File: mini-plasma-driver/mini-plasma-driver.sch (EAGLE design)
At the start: 82 parts, among them IC1 IR21844D, IC2 74LS19N, IC3 NE555N, IC4 NCP781IC, IC5 IR21844D, Q1 IRF640, Q2 IRF640, Q3 2N2369, Q4 2N2369, Q5 IRF640, Q6 IRF640

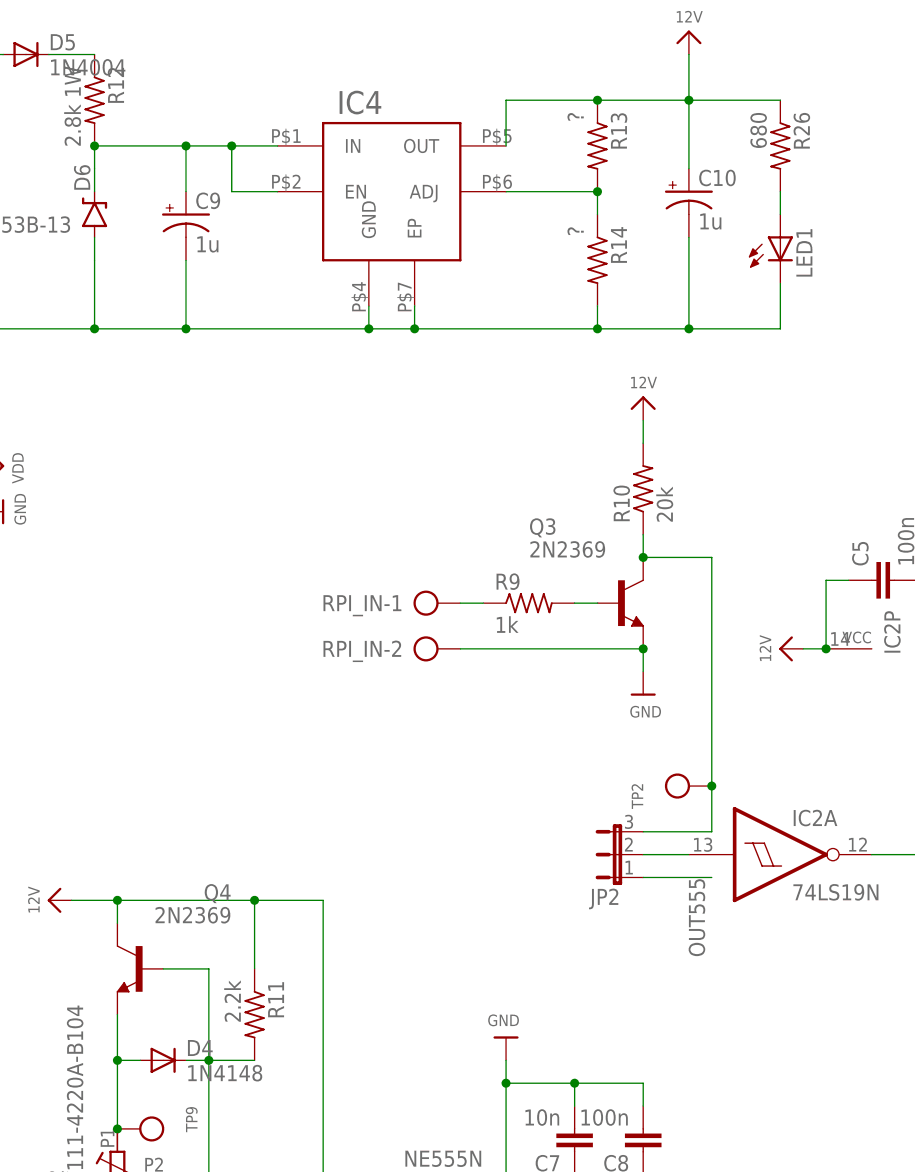
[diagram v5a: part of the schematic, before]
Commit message: C9 and C10 are not polarized
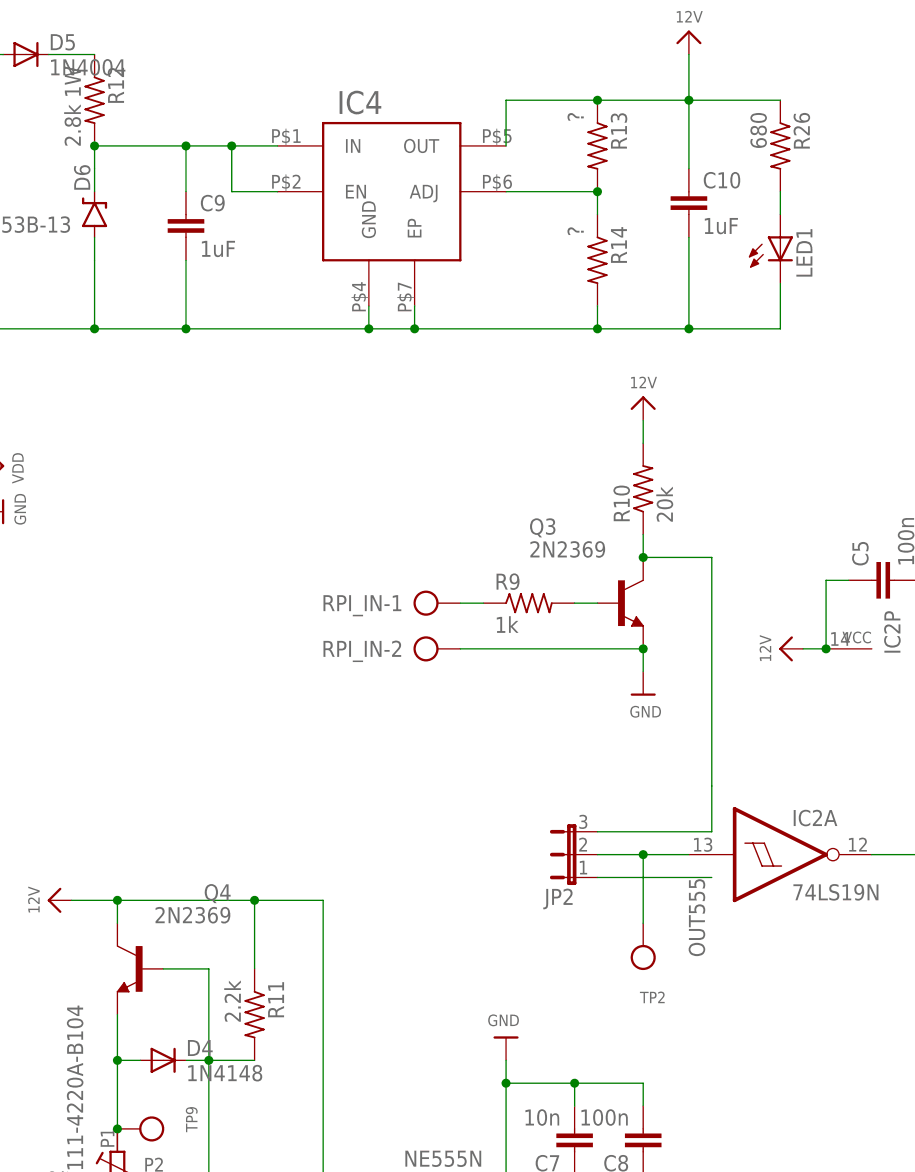
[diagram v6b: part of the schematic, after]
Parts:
- C10, C9: value 1u -> 1uF; device rcl:CPOL-USE2.5-5 -> rcl:C-EU025-025X050
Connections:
- net 12V: now also C10.1; no longer C10.+
- net GND: now also C10.2, C9.2; no longer C10.-, C9.-
- net N$12: no longer TP2.P$1
- net N$13: now also TP2.P$1
- net N$20: now also C9.1; no longer C9.+
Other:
- moved on the sheet: JP2, TP2
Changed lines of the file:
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@@
 <part name="GND3" library="microbuilder" deviceset="GND" device=""/>
 <part name="JP2" library="jumper" library_urn="urn:adsk.eagle:library:252" deviceset="JP2E" device="" package3d_urn="urn:adsk.eagle:package:15452/1"/>
-<part name="TP2" library="microbuilder" deviceset="TESTPOINT" device="0.1&quot;"/>
 <part name="IC2" library="74xx-eu" library_urn="urn:adsk.eagle:library:85" deviceset="74*19" device="N" package3d_urn="urn:adsk.eagle:package:2008/1" technology="LS"/>
 <part name="C5" library="rcl" library_urn="urn:adsk.eagle:library:334" deviceset="C-EU" device="025-025X050" package3d_urn="urn:adsk.eagle:package:23629/2" value="100n"/>
@@
 <part name="R12" library="rcl" library_urn="urn:adsk.eagle:library:334" deviceset="R-US_" device="0207/10" package3d_urn="urn:adsk.eagle:package:23491/1" value="2.8k 1W"/>
 <part name="D6" library="SparkFun-DiscreteSemi" deviceset="DIODE-ZENER" device="SMB" value="1SMB5953B-13"/>
-<part name="C9" library="rcl" library_urn="urn:adsk.eagle:library:334" deviceset="CPOL-US" device="E2.5-5" package3d_urn="urn:adsk.eagle:package:23344/1" value="1u"/>
 <part name="R13" library="rcl" library_urn="urn:adsk.eagle:library:334" deviceset="R-US_" device="0207/10" package3d_urn="urn:adsk.eagle:package:23491/1" value="?"/>
 <part name="R14" library="rcl" library_urn="urn:adsk.eagle:library:334" deviceset="R-US_" device="0207/10" package3d_urn="urn:adsk.eagle:package:23491/1" value="?"/>
-<part name="C10" library="rcl" library_urn="urn:adsk.eagle:library:334" deviceset="CPOL-US" device="E2.5-5" package3d_urn="urn:adsk.eagle:package:23344/1" value="1u"/>
 <part name="12V7" library="microbuilder" deviceset="12V" device=""/>
 <part name="GND7" library="microbuilder" deviceset="GND" device=""/>
@@
 <part name="TP8" library="microbuilder" deviceset="TESTPOINT" device="0.1&quot;"/>
 <part name="TP9" library="microbuilder" deviceset="TESTPOINT" device="0.1&quot;"/>
+<part name="TP2" library="microbuilder" deviceset="TESTPOINT" device="0.1&quot;"/>
+<part name="C9" library="rcl" library_urn="urn:adsk.eagle:library:334" deviceset="C-EU" device="025-025X050" package3d_urn="urn:adsk.eagle:package:23629/2" value="1uF"/>
+<part name="C10" library="rcl" library_urn="urn:adsk.eagle:library:334" deviceset="C-EU" device="025-025X050" package3d_urn="urn:adsk.eagle:package:23629/2" value="1uF"/>
 </parts>
 <sheets>
@@
 <instance part="12V3" gate="G$1" x="0" y="99.06"/>
 <instance part="GND3" gate="G$1" x="0" y="66.04"/>
-<instance part="JP2" gate="1" x="-2.54" y="48.26" rot="R90"/>
-<instance part="TP2" gate="G$1" x="7.62" y="55.88" rot="R90"/>
+<instance part="JP2" gate="1" x="-7.62" y="48.26" rot="R90"/>
 <instance part="IC2" gate="A" x="15.24" y="48.26"/>
 <instance part="IC2" gate="B" x="43.18" y="-10.16"/>
@@
 <attribute name="VALUE" x="-63.5" y="119.1514" size="1.778" layer="96" rot="R180"/>
 </instance>
-<instance part="C9" gate="G$1" x="-50.8" y="119.38"/>
 <instance part="R13" gate="G$1" x="-5.08" y="127" rot="R270"/>
 <instance part="R14" gate="G$1" x="-5.08" y="114.3" rot="R270"/>
-<instance part="C10" gate="G$1" x="5.08" y="121.92"/>
 <instance part="12V7" gate="G$1" x="5.08" y="139.7"/>
 <instance part="GND7" gate="G$1" x="-83.82" y="104.14"/>
@@
 <instance part="TP8" gate="G$1" x="-58.42" y="2.54" rot="R270"/>
 <instance part="TP9" gate="G$1" x="-58.42" y="17.78" rot="R270"/>
+<instance part="TP2" gate="G$1" x="0" y="40.64" rot="R180"/>
+<instance part="C9" gate="G$1" x="-50.8" y="119.38"/>
+<instance part="C10" gate="G$1" x="5.08" y="121.92"/>
 </instances>
 <busses>
@@
 <wire x1="-5.08" y1="132.08" x2="-15.24" y2="132.08" width="0.1524" layer="91"/>
 <wire x1="-15.24" y1="132.08" x2="-15.24" y2="127" width="0.1524" layer="91"/>
-<pinref part="C10" gate="G$1" pin="+"/>
 <wire x1="5.08" y1="124.46" x2="5.08" y2="132.08" width="0.1524" layer="91"/>
 <pinref part="R13" gate="G$1" pin="1"/>
@@
 <pinref part="R26" gate="G$1" pin="1"/>
 <wire x1="5.08" y1="132.08" x2="15.24" y2="132.08" width="0.1524" layer="91"/>
+<pinref part="C10" gate="G$1" pin="1"/>
 </segment>
 <segment>
@@
 <wire x1="-30.48" y1="109.22" x2="-30.48" y2="106.68" width="0.1524" layer="91"/>
 <wire x1="-60.96" y1="114.3" x2="-60.96" y2="106.68" width="0.1524" layer="91"/>
-<pinref part="C9" gate="G$1" pin="-"/>
 <wire x1="-50.8" y1="114.3" x2="-50.8" y2="106.68" width="0.1524" layer="91"/>
-<pinref part="C10" gate="G$1" pin="-"/>
 <wire x1="5.08" y1="116.84" x2="5.08" y2="106.68" width="0.1524" layer="91"/>
 <wire x1="5.08" y1="106.68" x2="-5.08" y2="106.68" width="0.1524" layer="91"/>
@@
 <wire x1="15.24" y1="106.68" x2="15.24" y2="111.76" width="0.1524" layer="91"/>
 <junction x="5.08" y="106.68"/>
+<pinref part="C9" gate="G$1" pin="2"/>
+<pinref part="C10" gate="G$1" pin="2"/>
 </segment>
 <segment>
@@
 <pinref part="JP2" gate="1" pin="3"/>
 <wire x1="7.62" y1="55.88" x2="7.62" y2="50.8" width="0.1524" layer="91"/>
-<wire x1="7.62" y1="50.8" x2="0" y2="50.8" width="0.1524" layer="91"/>
-<pinref part="TP2" gate="G$1" pin="P$1"/>
-<junction x="7.62" y="55.88"/>
+<wire x1="7.62" y1="50.8" x2="-5.08" y2="50.8" width="0.1524" layer="91"/>
 <junction x="0" y="81.28"/>
 </segment>
@@
 <wire x1="5.08" y1="48.26" x2="0" y2="48.26" width="0.1524" layer="91"/>
 <pinref part="IC2" gate="A" pin="I"/>
+<wire x1="0" y1="48.26" x2="-5.08" y2="48.26" width="0.1524" layer="91"/>
+<pinref part="TP2" gate="G$1" pin="P$1"/>
+<wire x1="0" y1="40.64" x2="0" y2="48.26" width="0.1524" layer="91"/>
+<junction x="0" y="48.26"/>
 </segment>
 </net>
@@
 <segment>
 <pinref part="JP2" gate="1" pin="1"/>
-<wire x1="0" y1="45.72" x2="7.62" y2="45.72" width="0.1524" layer="91"/>
+<wire x1="-5.08" y1="45.72" x2="7.62" y2="45.72" width="0.1524" layer="91"/>
 <label x="5.08" y="45.72" size="1.778" layer="95" rot="R270"/>
 </segment>
@@
 <wire x1="-50.8" y1="127" x2="-60.96" y2="127" width="0.1524" layer="91"/>
 <wire x1="-60.96" y1="127" x2="-60.96" y2="124.46" width="0.1524" layer="91"/>
-<pinref part="C9" gate="G$1" pin="+"/>
 <wire x1="-50.8" y1="121.92" x2="-50.8" y2="127" width="0.1524" layer="91"/>
 <pinref part="IC4" gate="G$1" pin="EN"/>
@@
 <pinref part="D6" gate="G$1" pin="C"/>
 <wire x1="-60.96" y1="124.46" x2="-60.96" y2="121.92" width="0.1524" layer="91"/>
-</segment>
-</net>
+<pinref part="C9" gate="G$1" pin="1"/>
+</segment>
+</net>

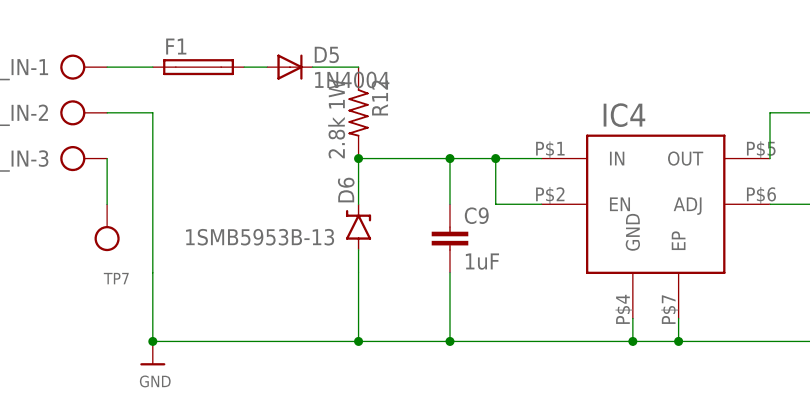
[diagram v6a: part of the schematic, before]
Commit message: Double up resistors R12, R27 and increased wattage
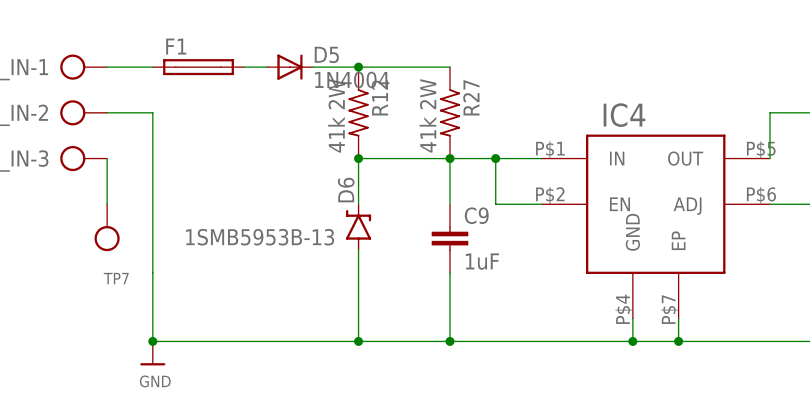
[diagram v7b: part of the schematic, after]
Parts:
- added R27: 41k 2W, rcl:R-US_0207/10
- R12: value 2.8k 1W -> 41k 2W
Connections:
- net N$19: now also R27.1
- net N$20: now also R27.2
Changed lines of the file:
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@@
 <part name="IC4" library="keves-ng" deviceset="NCP781" device="IC"/>
 <part name="D5" library="adafruit" deviceset="1N4004" device=""/>
-<part name="R12" library="rcl" library_urn="urn:adsk.eagle:library:334" deviceset="R-US_" device="0207/10" package3d_urn="urn:adsk.eagle:package:23491/1" value="2.8k 1W"/>
+<part name="R12" library="rcl" library_urn="urn:adsk.eagle:library:334" deviceset="R-US_" device="0207/10" package3d_urn="urn:adsk.eagle:package:23491/1" value="41k 2W"/>
 <part name="D6" library="SparkFun-DiscreteSemi" deviceset="DIODE-ZENER" device="SMB" value="1SMB5953B-13"/>
 <part name="R13" library="rcl" library_urn="urn:adsk.eagle:library:334" deviceset="R-US_" device="0207/10" package3d_urn="urn:adsk.eagle:package:23491/1" value="?"/>
@@
 <part name="C9" library="rcl" library_urn="urn:adsk.eagle:library:334" deviceset="C-EU" device="025-025X050" package3d_urn="urn:adsk.eagle:package:23629/2" value="1uF"/>
 <part name="C10" library="rcl" library_urn="urn:adsk.eagle:library:334" deviceset="C-EU" device="025-025X050" package3d_urn="urn:adsk.eagle:package:23629/2" value="1uF"/>
+<part name="R27" library="rcl" library_urn="urn:adsk.eagle:library:334" deviceset="R-US_" device="0207/10" package3d_urn="urn:adsk.eagle:package:23491/1" value="41k 2W"/>
 </parts>
 <sheets>
@@
 <instance part="C9" gate="G$1" x="-50.8" y="119.38"/>
 <instance part="C10" gate="G$1" x="5.08" y="121.92"/>
+<instance part="R27" gate="G$1" x="-50.8" y="132.08" rot="R270"/>
 </instances>
 <busses>
@@
 <pinref part="R12" gate="G$1" pin="1"/>
 <wire x1="-66.04" y1="137.16" x2="-60.96" y2="137.16" width="0.1524" layer="91"/>
+<pinref part="R27" gate="G$1" pin="1"/>
+<wire x1="-60.96" y1="137.16" x2="-50.8" y2="137.16" width="0.1524" layer="91"/>
+<junction x="-60.96" y="137.16"/>
 </segment>
 </net>
@@
 <wire x1="-60.96" y1="124.46" x2="-60.96" y2="121.92" width="0.1524" layer="91"/>
 <pinref part="C9" gate="G$1" pin="1"/>
-</segment>
-</net>
+<pinref part="R27" gate="G$1" pin="2"/>
+</segment>
+</net>
